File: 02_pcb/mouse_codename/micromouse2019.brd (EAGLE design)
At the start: 45 x 50 mm, 75 parts

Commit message: lib updated
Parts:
- moved PWR:C4 22.9 mm to (13.2, 4.96), turned to 180 degrees
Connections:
- net GND: no longer MOT:IC1.13
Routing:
- net GND: track 58.2 -> 67.9 mm, vias 8 -> 10
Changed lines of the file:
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@@
 <drawing>
 <settings>
-<setting alwaysvectorfont="yes"/>
+<setting alwaysvectorfont="no"/>
 <setting verticaltext="up"/>
 </settings>
@@
 <attribute name="VALUE" x="25.365" y="4.595" size="1.27" layer="27" rot="R90"/>
 </element>
-<element name="PWR:C4" library="0-micromouse2019" package="C0402" package3d_urn="urn:adsk.eagle:package:23626/2" value="1u" x="33.59" y="15.34" smashed="yes" rot="MR0">
-<attribute name="NAME" x="34.225" y="15.975" size="1.27" layer="26" rot="MR0"/>
-<attribute name="SPICEPREFIX" value="C" x="33.59" y="15.34" size="1.778" layer="28" rot="MR0" display="off"/>
-<attribute name="VALUE" x="34.225" y="13.435" size="1.27" layer="28" rot="MR0"/>
+<element name="PWR:C4" library="0-micromouse2019" package="C0402" package3d_urn="urn:adsk.eagle:package:23626/2" value="1u" x="13.16" y="4.96" smashed="yes" rot="MR180">
+<attribute name="NAME" x="12.525" y="4.325" size="1.27" layer="26" rot="MR180"/>
+<attribute name="SPICEPREFIX" value="C" x="13.16" y="4.96" size="1.778" layer="28" rot="MR180" display="off"/>
+<attribute name="VALUE" x="12.525" y="6.865" size="1.27" layer="28" rot="MR180"/>
 </element>
 <element name="PWR:C5" library="0-micromouse2019" package="C0402" package3d_urn="urn:adsk.eagle:package:23626/2" value="10u" x="15.52" y="8.06" smashed="yes">
@@
 <contactref element="MCU:J1" pad="3"/>
 <contactref element="MOT:C1" pad="2"/>
-<contactref element="MOT:IC1" pad="13"/>
 <contactref element="MOT:IC1" pad="14"/>
 <contactref element="MOT:IC1" pad="16"/>
@@
 <wire x1="15.45" y1="7.1" x2="16.17" y2="8.06" width="0.5" layer="1"/>
 <wire x1="16.4315" y1="6.409" x2="17.35" y2="6.4" width="0.27" layer="1"/>
-<polygon width="0.1524" layer="16" pour="cutout" rank="3">
+<polygon width="0.1524" layer="16" pour="cutout" isolate="0.3048" rank="3">
 <vertex x="0" y="0"/>
 <vertex x="45" y="0"/>
@@
 <contactref element="MCU:R8" pad="2"/>
 <contactref element="MCU:R9" pad="2"/>
+<via x="20.42" y="21.54" extent="1-16" drill="0.3" diameter="0.6"/>
+<via x="21.28" y="21.54" extent="1-16" drill="0.3" diameter="0.6"/>
+<polygon width="0.1" layer="1" spacing="0.5" isolate="0.254">
+<vertex x="19.95" y="21.9"/>
+<vertex x="21.75" y="21.9"/>
+<vertex x="21.75" y="21.15"/>
+<vertex x="19.95" y="21.15"/>
+</polygon>
+<wire x1="19.4874" y1="21.29" x2="22.2246" y2="21.29" width="0.27" layer="1"/>
+<wire x1="19.4874" y1="21.79" x2="22.2246" y2="21.79" width="0.27" layer="1"/>
+<wire x1="22.2246" y1="21.29" x2="21.53" y2="21.29" width="0.27" layer="1"/>
+<wire x1="21.53" y1="21.29" x2="21.285" y2="21.535" width="0.27" layer="1"/>
+<wire x1="21.285" y1="21.535" x2="21.28" y2="21.54" width="0.27" layer="1"/>
+<wire x1="22.2246" y1="21.79" x2="21.54" y2="21.79" width="0.27" layer="1"/>
+<wire x1="21.54" y1="21.79" x2="21.285" y2="21.535" width="0.27" layer="1"/>
+<wire x1="20.42" y1="21.54" x2="20.17" y2="21.29" width="0.27" layer="1"/>
+<wire x1="20.17" y1="21.29" x2="19.4874" y2="21.29" width="0.27" layer="1"/>
+<wire x1="20.42" y1="21.54" x2="20.17" y2="21.79" width="0.27" layer="1"/>
+<wire x1="20.17" y1="21.79" x2="19.4874" y2="21.79" width="0.27" layer="1"/>
 <wire x1="38" y1="36.7" x2="38" y2="38.3" width="0" layer="19" extent="16-16"/>
 <wire x1="38" y1="40" x2="38" y2="38.3" width="0" layer="19" extent="16-16"/>
@@
 <wire x1="9.8" y1="47.7" x2="9.75" y2="46.2" width="0" layer="19" extent="16-16"/>
 <wire x1="16.5" y1="23.35" x2="18.54" y2="28.74" width="0" layer="19" extent="1-16"/>
-<wire x1="18.273" y1="21.79" x2="16.5" y2="23.35" width="0" layer="19" extent="1-1"/>
-<wire x1="20.856" y1="21.54" x2="19.4874" y2="21.79" width="0" layer="19" extent="1-1"/>
-<wire x1="22.2246" y1="21.79" x2="20.856" y2="21.54" width="0" layer="19" extent="1-1"/>
-<wire x1="23.61" y1="21.29" x2="23.63" y2="21.79" width="0" layer="19" extent="1-1"/>
+<wire x1="17.973" y1="21.49" x2="16.5" y2="23.35" width="0" layer="19" extent="1-1"/>
 <wire x1="22.106" y1="20.5444" x2="22.2246" y2="21.29" width="0" layer="19" extent="1-1"/>
 <wire x1="26.7" y1="23.7" x2="23.86" y2="22.02" width="0" layer="19" extent="1-1"/>
 <wire x1="26.11" y1="11.84" x2="23.297" y2="19.647" width="0" layer="19" extent="1-1"/>
 <wire x1="23.25" y1="6.45" x2="26.11" y2="11.84" width="0" layer="19" extent="1-1"/>
-<wire x1="18.89" y1="7.94" x2="21.144" y2="6.674" width="0" layer="19" extent="1-1"/>
-<wire x1="17.35" y1="6.4" x2="18.89" y2="7.94" width="0" layer="19" extent="1-1"/>
-<wire x1="32.94" y1="15.34" x2="26.11" y2="11.84" width="0" layer="19" extent="1-16"/>
+<wire x1="13.81" y1="4.96" x2="14.02" y2="3.69" width="0" layer="19" extent="16-16"/>
+<wire x1="15.444" y1="6.409" x2="13.81" y2="4.96" width="0" layer="19" extent="1-16"/>
+<wire x1="18.89" y1="7.94" x2="17.35" y2="6.4" width="0" layer="19" extent="1-1"/>
 <wire x1="15.75" y1="56.8" x2="20.385" y2="48.379" width="0" layer="19" extent="1-16"/>
 <wire x1="14.7" y1="56.8" x2="15.75" y2="56.8" width="0" layer="19" extent="16-16"/>
 <wire x1="13.6" y1="56.8" x2="14.7" y2="56.8" width="0" layer="19" extent="16-16"/>
-<wire x1="36.15" y1="5.25" x2="32.94" y2="15.34" width="0" layer="19" extent="1-16"/>
+<wire x1="36.15" y1="5.25" x2="26.11" y2="11.84" width="0" layer="19" extent="1-1"/>
 <wire x1="36.72" y1="1.67" x2="36.15" y2="5.25" width="0" layer="19" extent="1-1"/>
 </signal>
@@
 <contactref element="PWR:LDO1" pad="4"/>
 <contactref element="PWR:LDO1" pad="6"/>
-<wire x1="20.1026" y1="5.8634" x2="34.24" y2="15.34" width="0" layer="19" extent="1-16"/>
+<wire x1="12.87" y1="5" x2="12.51" y2="4.96" width="0" layer="19" extent="1-16"/>
 </signal>
 <signal name="DRV_A_IN1">

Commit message: pcb route 4th phase
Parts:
- moved MCU:C13 36.0 mm to (1.86, 6.06)
- moved MCU:C12 34.5 mm to (9.60, 1.87), turned to 270 degrees
- moved IRD2:CONN2 32.7 mm to (35.5, 34.4)
- moved IRD2:R5 10.1 mm to (12.4, 35.4)
- moved MCU:R3 10.0 mm to (34.5, 32.1), turned to 0 degrees
- moved IRD2:R6 9.88 mm to (12.4, 34.4)
- moved MCU:R1 6.69 mm to (38.7, 4.73)
- moved IRD1:R2 5.27 mm to (8.25, 42.6), turned to 180 degrees
- moved MCU:C9 3.04 mm to (25.1, 27.5)
- moved MCU:C3 3.04 mm to (25.1, 28.6)
- moved MCU:C1 2.51 mm to (17.0, 36.6), turned to 0 degrees
- moved IRD1:CONN2 2.20 mm to (4.05, 31.6)
- moved MCU:C2 2.19 mm to (19.9, 31.6), turned to 180 degrees
- moved IRD2:R2 1.90 mm to (9.25, 45.8)
- moved MCU:C8 1.75 mm to (19.9, 30.5), turned to 180 degrees
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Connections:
- net GND: now also IMU:IC1.15, IMU:IC1.5
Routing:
- net +3V3: track 80.2 -> 170.5 mm, vias 7 -> 17
- net VCC: track 56.1 -> 115.2 mm, vias 0 -> 4
- net GND: track 67.9 -> 116.0 mm, vias 10 -> 38
- net MCU:NRST: track 0.00 -> 13.9 mm, vias 0 -> 1
- net N$2: track 0.00 -> 9.66 mm
- net UART3_RX: track 32.5 -> 37.5 mm
- net IMU:REGOUT: track 1.17 -> 5.82 mm, vias 0 -> 1
- net MCU:BTN_BOOT0: track 0.00 -> 4.41 mm, vias 0 -> 1
- net MCU:V_BAT: track 0.00 -> 3.73 mm, vias 0 -> 1
- net N$6: track 0.00 -> 3.64 mm
- net BT_PORT:BT_STATUS: track 0.00 -> 3.59 mm
- net UART3_TX: track 33.5 -> 36.4 mm
- net PWR:V_BAT_IN: track 16.9 -> 19.6 mm
- net MCU:BTN1: track 32.9 -> 34.9 mm, vias 2 -> 3
- net IMU:AD0: track 2.88 -> 4.35 mm
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- added copper zone on layer 1, net +3V3
- added copper zone on layer 16, net +3V3
- added copper zone on layer 16, net VCC

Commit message: pcb routing alpha v1_0
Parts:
- moved IRD1:R5 23.5 mm to (11.8, 34.1)
- moved IRD1:R6 23.2 mm to (13.0, 34.1)
- moved IRD1:R1 17.9 mm to (11.4, 39.5), turned to 180 degrees
- moved IRD2:R6 8.09 mm to (14.2, 42.2), turned to 270 degrees
- moved IRD2:R5 6.87 mm to (13.0, 42.2), turned to 270 degrees
- moved IRD1:CONN2 6.08 mm to (9.55, 34.2)
- moved IRD1:R2 4.67 mm to (6.55, 38.2)
- moved IRD2:R2 4.59 mm to (6.60, 42.0), turned to 180 degrees
- moved IRD1:MOSFET1 2.61 mm to (9.70, 38.5), turned to 180 degrees
- moved IRD2:R1 2.46 mm to (11.4, 43.5), turned to 180 degrees
- moved IRD2:CONN1 2.45 mm to (9.85, 40.6), turned to 0 degrees
- moved IRD1:CONN1 2.23 mm to (9.90, 36.7), turned to 0 degrees
- moved IRD2:MOSFET1 1.92 mm to (9.65, 42.4), turned to 180 degrees
- moved IMU:R1 1.09 mm to (24.0, 41.3), flipped to the bottom, turned to 180 degrees
- moved MCU:C11 0.96 mm to (20.9, 44.2)
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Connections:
- net IRD1:N$1 renamed IRD1:DRAIN_1
- net IRD2:N$1 renamed IRD2:DRAIN_1
- removed net IRD1:N$2: IRD1:CONN1.3, IRD1:MOSFET1.P3
- removed net IRD2:N$2: IRD2:CONN1.3, IRD2:MOSFET1.P3
- new net IRD1:DRAIN_2: IRD1:CONN1.2, IRD1:MOSFET1.P3
- new net IRD2:DRAIN_2: IRD2:CONN1.2, IRD2:MOSFET1.P3
- net N$1: now also MCU:IC1.14; no longer MCU:IC1.16
- net N$2: now also MCU:IC1.15; no longer MCU:IC1.17
- net N$3: now also IRD1:CONN1.3, MCU:IC1.16; no longer IRD1:CONN1.2, MCU:IC1.14
- net N$4: now also MCU:IC1.17; no longer MCU:IC1.15
- net N$7: now also IRD2:CONN1.3; no longer IRD2:CONN1.2
- net V_BAT_LEVEL: now also MCU:IC1.22; no longer MCU:IC1.20
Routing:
- net N$6: track 3.64 -> 22.1 mm, vias 0 -> 1
- net N$5: track 0.00 -> 17.1 mm, vias 0 -> 2
- net N$7: track 0.00 -> 15.3 mm
- net N$1: track 0.00 -> 14.5 mm, vias 0 -> 2
- net N$8: track 0.00 -> 13.4 mm
- net N$3: track 0.00 -> 12.7 mm
- net N$2: track 9.66 -> 18.7 mm, vias 0 -> 1
- net N$4: track 0.00 -> 5.98 mm
- net IRD2:DRAIN_2: track 0.00 -> 4.69 mm
- net IRD1:DRAIN_2: track 0.00 -> 4.69 mm
- net IRD1:DRAIN_1: track 0.00 -> 3.46 mm
- net IRD2:DRAIN_1: track 0.00 -> 3.22 mm
- net +3V3: track 170.5 -> 167.5 mm, vias 17 -> 16
- net GND: track 116.0 -> 118.4 mm, vias 38 -> 48
- net V_BAT_LEVEL: track 39.1 -> 38.1 mm
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
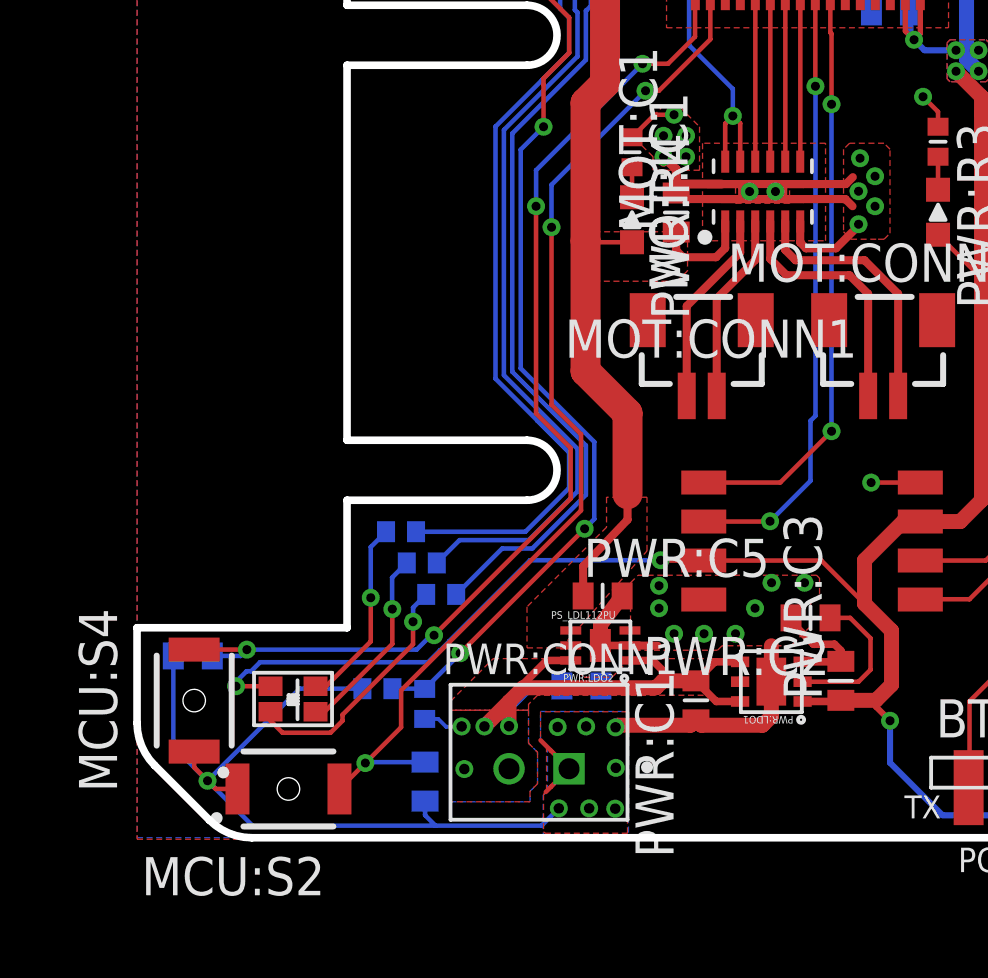
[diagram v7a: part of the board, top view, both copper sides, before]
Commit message: button fix, drv8836 exposed pad fix
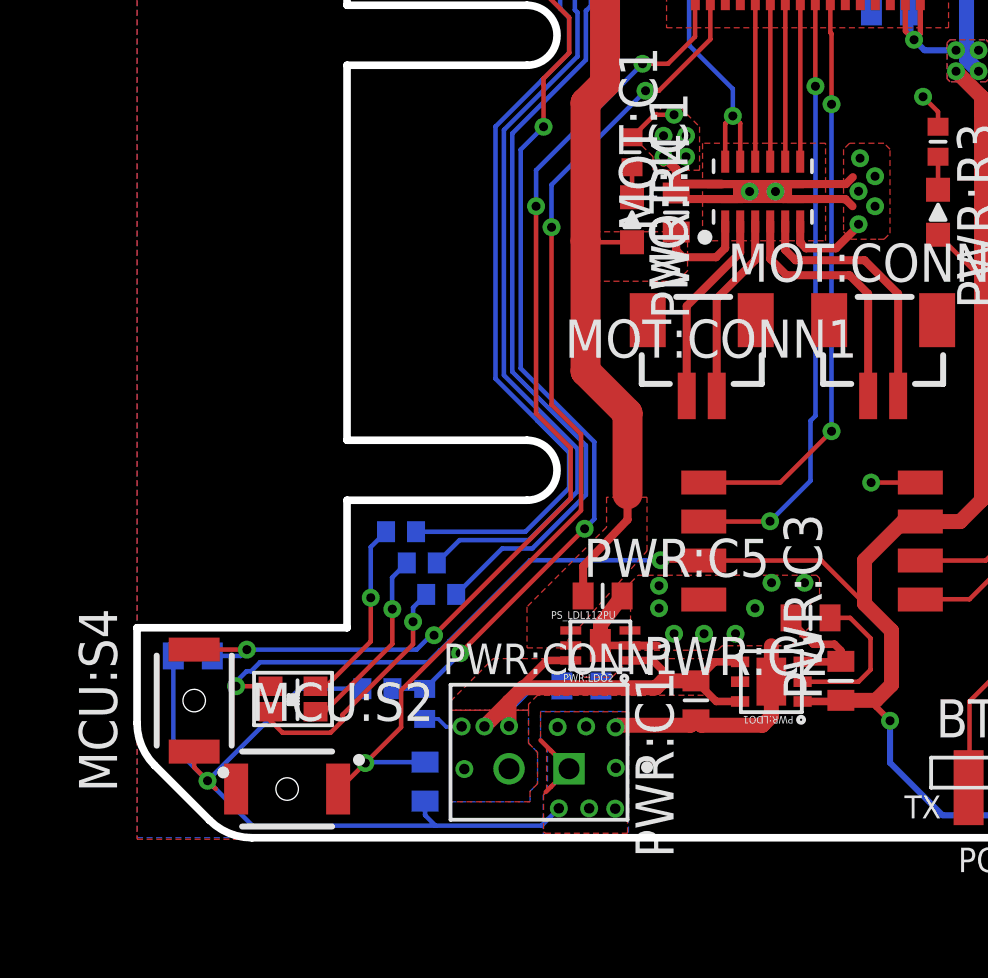
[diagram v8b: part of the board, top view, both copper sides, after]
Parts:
- turned MCU:S2 to 0 degrees
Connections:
- net GND: now also MCU:S2.2; no longer MCU:S2.1
- net MCU:BTN1: now also MCU:S2.1; no longer MCU:S2.2
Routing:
- net GND: track 118.4 -> 120.7 mm
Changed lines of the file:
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@@
 <layer number="23" name="tOrigins" color="15" fill="1" visible="yes" active="yes"/>
 <layer number="24" name="bOrigins" color="15" fill="1" visible="yes" active="yes"/>
-<layer number="25" name="tNames" color="7" fill="1" visible="no" active="yes"/>
-<layer number="26" name="bNames" color="7" fill="1" visible="no" active="yes"/>
-<layer number="27" name="tValues" color="7" fill="1" visible="no" active="yes"/>
+<layer number="25" name="tNames" color="7" fill="1" visible="yes" active="yes"/>
+<layer number="26" name="bNames" color="7" fill="1" visible="yes" active="yes"/>
+<layer number="27" name="tValues" color="7" fill="1" visible="yes" active="yes"/>
 <layer number="28" name="bValues" color="7" fill="1" visible="no" active="yes"/>
 <layer number="29" name="tStop" color="7" fill="3" visible="no" active="yes"/>
@@
 </layers>
 <board>
-<fusionsync huburn="a.cGVyc29uYWw6dWUyOWUzYzUy" projecturn="a.cGVyc29uYWw6dWUyOWUzYzUyIzIwMTkwMjExMTc1NjcyODUx" f3durn="urn:adsk.wipprod:dm.lineage:jzhWZ2RJTSK-yRQwBFZECw" pcbguid="c2b5e295-5b88-443b-b552-b85fb43e7534" lastpulledtime="2019-02-22T16:16:36Z" lastsyncedchangeguid="e1eb7793-ca3e-f807-a688-d96406854a24"/>
+<fusionsync huburn="a.cGVyc29uYWw6dWUyOWUzYzUy" projecturn="a.cGVyc29uYWw6dWUyOWUzYzUyIzIwMTkwMjExMTc1NjcyODUx" f3durn="urn:adsk.wipprod:dm.lineage:jzhWZ2RJTSK-yRQwBFZECw" pcbguid="c2b5e295-5b88-443b-b552-b85fb43e7534" lastpulledtime="2019-02-22T16:16:36Z" lastsyncedchangeguid="0656dba7-2336-cb5f-136f-0c0dbd84525e"/>
 <plain>
 <rectangle x1="6.858" y1="11.303" x2="13.589" y2="27.813" layer="39"/>
@@
 <attribute name="VALUE" x="18.224" y="48.173" size="1.27" layer="27" align="center"/>
 </element>
-<element name="MCU:S2" library="0-micromouse2019" package="B3U-3000P" package3d_urn="urn:adsk.eagle:package:8879469/3" value="BTN1" x="5.047" y="1.626" smashed="yes" rot="R180">
-<attribute name="NAME" x="3.208" y="-1.281" size="1.27" layer="25" rot="R180" align="center"/>
-<attribute name="VALUE" x="7.963" y="2.385" size="1.27" layer="27" rot="R270" align="center"/>
+<element name="MCU:S2" library="0-micromouse2019" package="B3U-3000P" package3d_urn="urn:adsk.eagle:package:8879469/3" value="BTN1" x="5.003" y="1.624" smashed="yes">
+<attribute name="NAME" x="6.842" y="4.531" size="1.27" layer="25" align="center"/>
+<attribute name="VALUE" x="2.087" y="0.865" size="1.27" layer="27" rot="R90" align="center"/>
 </element>
 <element name="MCU:S3" library="0-micromouse2019" package="B3U-1000P" package3d_urn="urn:adsk.eagle:package:8879289/5" value="BTN_B3U-1000P" x="42.164" y="2.921" smashed="yes" rot="R45">
@@
 </signal>
 <signal name="MCU:BTN1">
-<contactref element="MCU:S2" pad="2"/>
 <contactref element="MCU:C12" pad="1"/>
 <wire x1="8.802" y1="4.912" x2="8.802" y2="3.681" width="0.1524" layer="1"/>
-<wire x1="6.747" y1="1.626" x2="7.6105" y2="2.4895" width="0.1524" layer="1"/>
 <wire x1="7.6105" y1="2.4895" x2="8.802" y2="3.681" width="0.1524" layer="1"/>
 <wire x1="8.802" y1="4.912" x2="14.8" y2="10.91" width="0.1524" layer="1"/>
@@
 <wire x1="7.641" y1="2.52" x2="7.6105" y2="2.4895" width="0.1524" layer="16"/>
 <via x="7.6105" y="2.4895" extent="1-16" drill="0.3" diameter="0.6"/>
+<contactref element="MCU:S2" pad="1"/>
+<wire x1="7.6105" y1="2.4895" x2="6.745" y2="1.624" width="0.1524" layer="1"/>
+<wire x1="6.745" y1="1.624" x2="6.703" y2="1.624" width="0.1524" layer="1"/>
 </signal>
 <signal name="MCU:IMU2_SCL">
@@
 <contactref element="MCU:C13" pad="2"/>
 <contactref element="MCU:C12" pad="2"/>
-<contactref element="MCU:S2" pad="1"/>
 <contactref element="MCU:J1" pad="3"/>
 <contactref element="MOT:C1" pad="2"/>
@@
 <wire x1="1.905" y1="2.345" x2="1.905" y2="2.872" width="0.1524" layer="1"/>
 <wire x1="2.35" y1="1.9" x2="2.624" y2="1.626" width="0.1524" layer="1"/>
-<wire x1="2.624" y1="1.626" x2="3.347" y2="1.626" width="0.1524" layer="1"/>
 <wire x1="22.1854" y1="5.8634" x2="23.4434" y2="5.8634" width="0.254" layer="1"/>
 <wire x1="23.4434" y1="5.8634" x2="23.46" y2="5.88" width="0.254" layer="1"/>
@@
 <via x="20.42" y="21.54" extent="1-16" drill="0.3" diameter="0.6"/>
 <via x="21.28" y="21.54" extent="1-16" drill="0.3" diameter="0.6"/>
-<polygon width="0.1" layer="1" spacing="0.5" isolate="0.254">
-<vertex x="19.95" y="21.9"/>
-<vertex x="21.75" y="21.9"/>
-<vertex x="21.75" y="21.15"/>
-<vertex x="19.95" y="21.15"/>
-</polygon>
-<wire x1="19.4874" y1="21.29" x2="20.17" y2="21.29" width="0.27" layer="1"/>
+<wire x1="19.4874" y1="21.29" x2="20" y2="21.29" width="0.27" layer="1"/>
+<wire x1="20" y1="21.29" x2="20.17" y2="21.29" width="0.27" layer="1"/>
 <wire x1="20.17" y1="21.29" x2="21.53" y2="21.29" width="0.27" layer="1"/>
-<wire x1="21.53" y1="21.29" x2="22.2246" y2="21.29" width="0.27" layer="1"/>
-<wire x1="19.4874" y1="21.79" x2="22.2246" y2="21.79" width="0.27" layer="1"/>
-<wire x1="22.2246" y1="21.29" x2="21.53" y2="21.29" width="0.27" layer="1"/>
+<wire x1="21.53" y1="21.29" x2="21.7" y2="21.29" width="0.27" layer="1"/>
+<wire x1="21.7" y1="21.29" x2="22.2246" y2="21.29" width="0.27" layer="1"/>
+<wire x1="19.4874" y1="21.79" x2="20" y2="21.79" width="0.27" layer="1"/>
+<wire x1="20" y1="21.79" x2="21.75" y2="21.79" width="0.27" layer="1"/>
+<wire x1="21.75" y1="21.79" x2="22.2246" y2="21.79" width="0.27" layer="1"/>
+<wire x1="22.2246" y1="21.29" x2="21.7" y2="21.29" width="0.27" layer="1"/>
+<wire x1="21.7" y1="21.29" x2="21.53" y2="21.29" width="0.27" layer="1"/>
 <wire x1="21.53" y1="21.29" x2="21.285" y2="21.535" width="0.27" layer="1"/>
 <wire x1="21.285" y1="21.535" x2="21.28" y2="21.54" width="0.27" layer="1"/>
-<wire x1="22.2246" y1="21.79" x2="21.54" y2="21.79" width="0.27" layer="1"/>
+<wire x1="22.2246" y1="21.79" x2="21.75" y2="21.79" width="0.27" layer="1"/>
 <wire x1="21.54" y1="21.79" x2="21.285" y2="21.535" width="0.27" layer="1"/>
-<wire x1="20.17" y1="21.29" x2="19.4874" y2="21.29" width="0.27" layer="1"/>
-<wire x1="19.4874" y1="21.79" x2="20.17" y2="21.79" width="0.27" layer="1"/>
+<wire x1="20.17" y1="21.29" x2="20" y2="21.29" width="0.27" layer="1"/>
+<wire x1="20" y1="21.29" x2="19.4874" y2="21.29" width="0.27" layer="1"/>
+<wire x1="19.4874" y1="21.79" x2="20" y2="21.79" width="0.27" layer="1"/>
+<wire x1="20" y1="21.79" x2="20.17" y2="21.79" width="0.27" layer="1"/>
 <wire x1="26.11" y1="11.84" x2="24.47" y2="11.84" width="0.1524" layer="1"/>
 <via x="24.47" y="11.84" extent="1-16" drill="0.3" diameter="0.6"/>
@@
 <wire x1="21.54" y1="21.79" x2="21.54" y2="21.3" width="0.27" layer="1"/>
 <wire x1="21.54" y1="21.3" x2="21.53" y2="21.29" width="0.27" layer="1"/>
-<wire x1="20.17" y1="21.79" x2="20.17" y2="21.29" width="0.27" layer="1"/>
+<wire x1="20.17" y1="21.79" x2="20.17" y2="21.75" width="0.27" layer="1"/>
 <via x="24.05" y="21.55" extent="1-16" drill="0.3" diameter="0.6"/>
 <via x="24.05" y="20.45" extent="1-16" drill="0.3" diameter="0.6"/>
@@
 <via x="24.6" y="22.05" extent="1-16" drill="0.3" diameter="0.6"/>
 <via x="24.1" y="22.65" extent="1-16" drill="0.3" diameter="0.6"/>
+<wire x1="20.17" y1="21.75" x2="20.17" y2="21.29" width="0.27" layer="1"/>
 <wire x1="26.7" y1="23.7" x2="26.7" y2="24.2" width="0.1524" layer="1"/>
 <wire x1="26.7" y1="24.2" x2="26.2" y2="24.7" width="0.1524" layer="1"/>
@@
 <vertex x="22.95" y="23.15"/>
 </polygon>
+<contactref element="MCU:S2" pad="2"/>
+<wire x1="20.42" y1="21.54" x2="20.425" y2="21.535" width="0.7" layer="1"/>
+<wire x1="20.425" y1="21.535" x2="21.285" y2="21.535" width="0.7" layer="1"/>
+<wire x1="20.42" y1="21.54" x2="20.17" y2="21.79" width="0.27" layer="1"/>
+<wire x1="20.17" y1="21.79" x2="20" y2="21.79" width="0.27" layer="1"/>
+<wire x1="20.17" y1="21.75" x2="20" y2="21.75" width="0.27" layer="1"/>
+<wire x1="20" y1="21.75" x2="20" y2="21.29" width="0.27" layer="1"/>
+<wire x1="21.54" y1="21.79" x2="21.75" y2="21.79" width="0.27" layer="1"/>
+<wire x1="22.2246" y1="21.79" x2="21.7" y2="21.79" width="0.27" layer="1"/>
+<wire x1="21.7" y1="21.79" x2="21.7" y2="21.29" width="0.27" layer="1"/>
 </signal>
 <signal name="+3V3">
